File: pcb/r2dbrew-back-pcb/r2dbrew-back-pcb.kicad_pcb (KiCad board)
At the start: 2 copper layers, 120.7 x 41.3 mm, 152 parts, among them IC1 74HC238, IC2 TLC5971, IC3 FT230X, IC4 LM1117, IC5 ATMEGA328P, J1 USB, J2 PSI1, J3 PSI2, J4 RGB1, J5 RGB2, J6 6-12V, P1 AVR_ISP, Q1 DDTD113ZC, Q10 DDTB113ZC, Q11 DDTB113ZC, Q12 DDTB113ZC, Q13 DDTB113ZC, Q14 DDTB113ZC, Q15 DDTB113ZC, Q16 DDTB113ZC, Q17 DDTB113ZC, Q18 DDTB113ZC, Q19 DDTB113ZC, Q2 DDTD113ZC, Q3 DDTD113ZC, Q4 DDTD113ZC, Q5 DDTD113ZC, Q6 DDTD113ZC, Q7 DDTD113ZC, Q8 DDTD113ZC, Q9 DDTB113ZC, Y1 16MHz

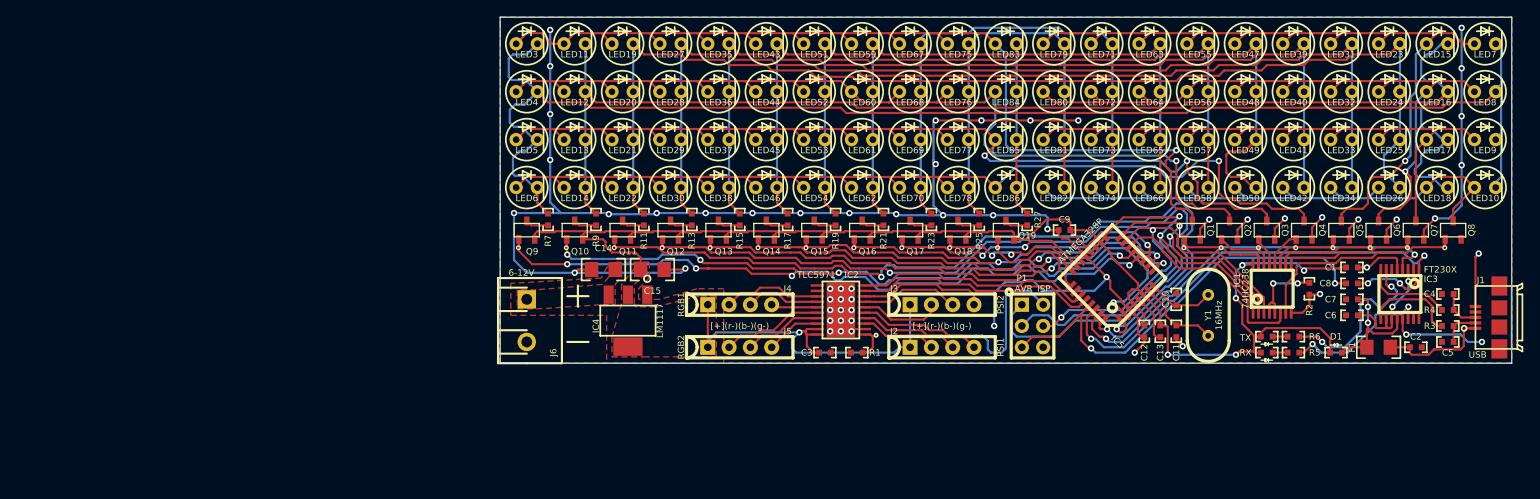
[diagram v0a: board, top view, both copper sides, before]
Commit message: cleanup after project rename
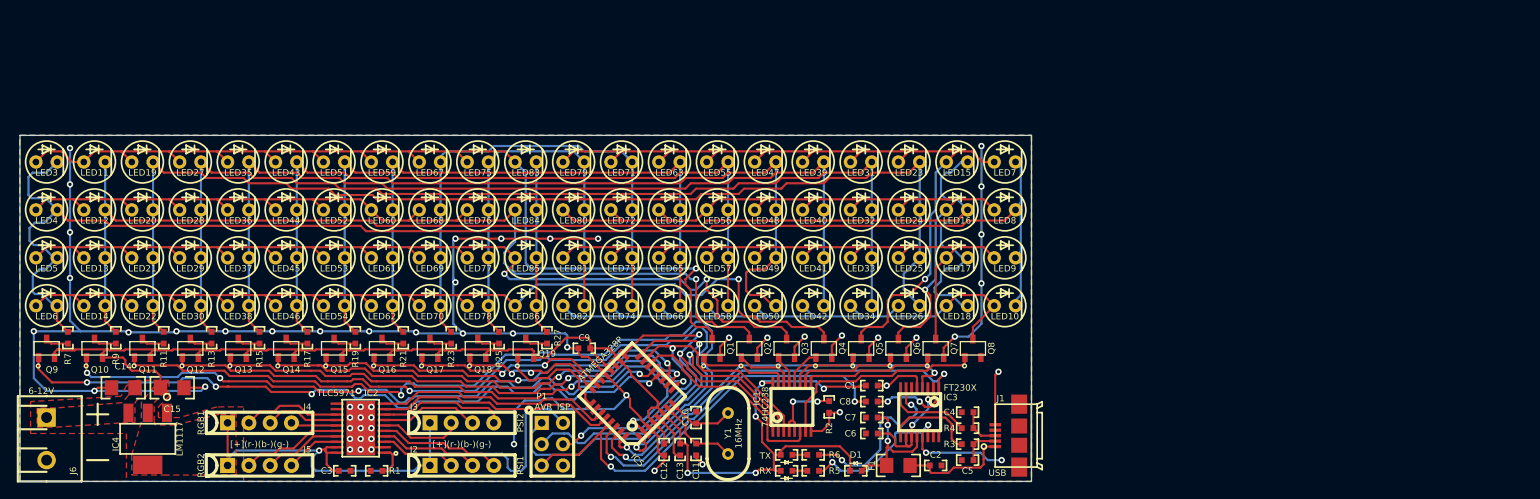
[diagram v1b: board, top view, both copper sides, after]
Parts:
- moved C10 59.0 mm to (156.1, 124.0)
- moved C11 59.0 mm to (156.1, 127.8)
- moved C12 59.0 mm to (152.3, 127.8)
- moved C13 59.0 mm to (154.2, 127.8)
- moved C2 59.0 mm to (184.7, 129.7)
- moved C4 59.0 mm to (188.5, 123.3)
- moved C5 59.0 mm to (188.5, 129.0)
- moved C9 59.0 mm to (142.7, 115.7)
- moved F1 59.0 mm to (180.2, 129.7)
- moved IC3 59.0 mm to (182.8, 123.3)
- moved IC4 59.0 mm to (90.7, 126.5)
- moved IC5 59.0 mm to (148.5, 121.4)
- moved J1 59.0 mm to (194.6, 126.1)
- moved LED1 59.0 mm to (166.9, 130.3)
- moved LED2 59.0 mm to (166.9, 128.4)
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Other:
- board size 120.7 x 41.3 mm -> 120.6 x 41.3 mm

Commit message: fix mask clearance for back board
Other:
- rule pad_to_mask_clearance: 0 -> 0.0762

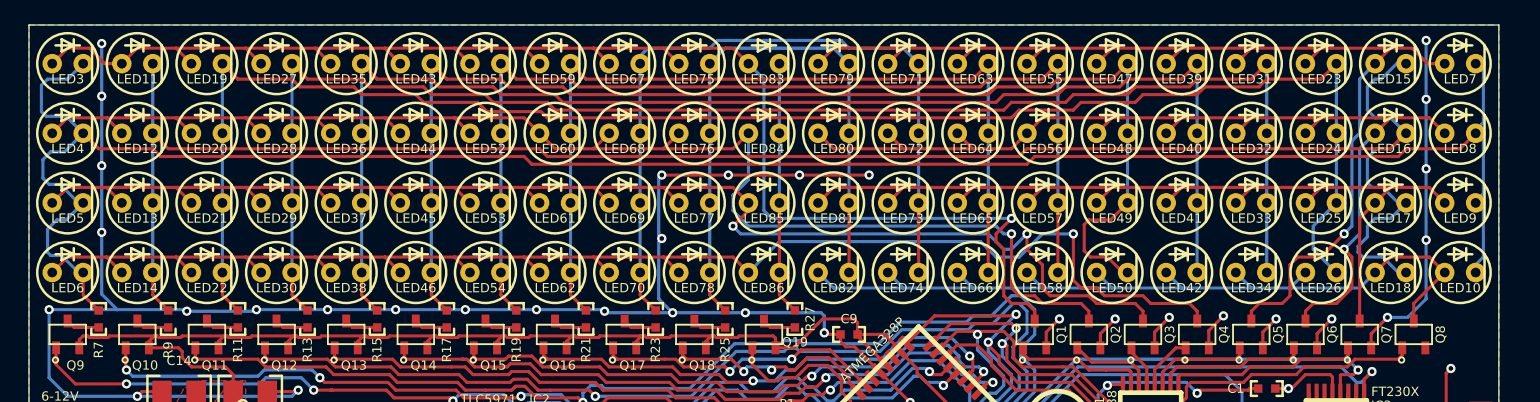
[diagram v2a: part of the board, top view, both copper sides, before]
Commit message: switch back leds to proper orientation. fixes #1
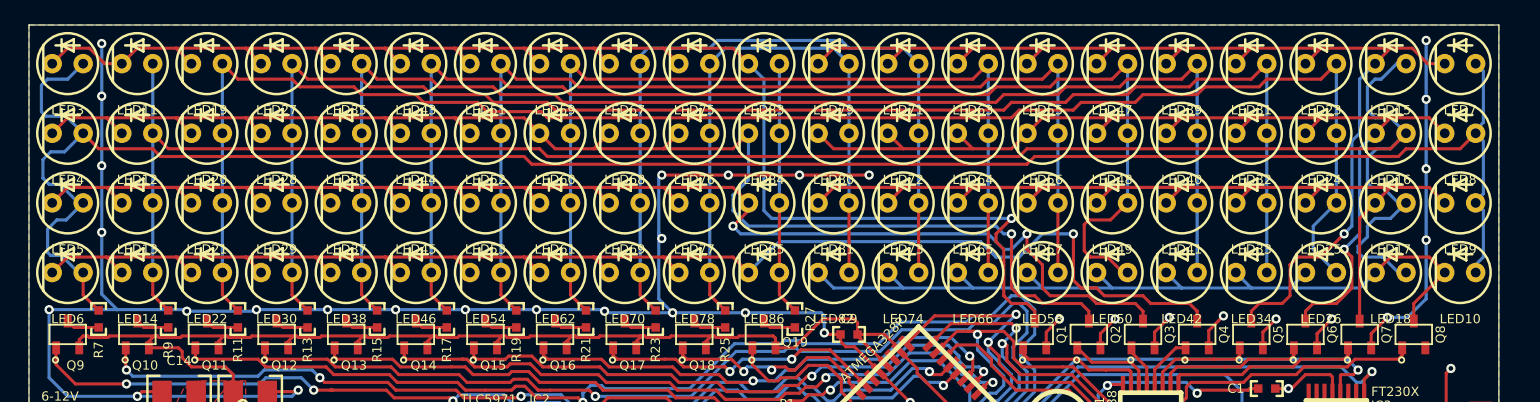
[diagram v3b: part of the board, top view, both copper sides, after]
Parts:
- LED10, LED11, LED12, LED13, LED14, LED15, LED16, LED17, LED18, LED19, LED20, LED21, LED22, LED23, LED24, LED25, LED26, LED27, LED28, LED29, LED3, LED30, LED31, LED32, LED33, LED34, LED35, LED36, LED37, LED38, LED39, LED4, LED40, LED41, LED42, LED43, LED44, LED45, LED46, LED47, LED48, LED49, LED5, LED50, LED51, LED52, LED53, LED54, LED55, LED56, LED57, LED58, LED59, LED6, LED60, LED61, LED62, LED63, LED64, LED65, LED66, LED67, LED68, LED69, LED7, LED70, LED71, LED72, LED73, LED74, LED75, LED76, LED77, LED78, LED79, LED8, LED80, LED81, LED82, LED83, LED84, LED85, LED86, LED9: footprint th leds:LED-5mm -> led:5mm-THRU-LED
